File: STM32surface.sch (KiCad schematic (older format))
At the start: 25 parts, among them J3 USB_B, J4 Conn_01x04, J5 Conn_01x20, J6 Conn_02x03_Odd_Even, J7 Conn_01x02, J9 Conn_01x20, U1 AMS1117-3V3, U2 STM32F103C8T6, Y1 8 MHz, Y2 Crystal

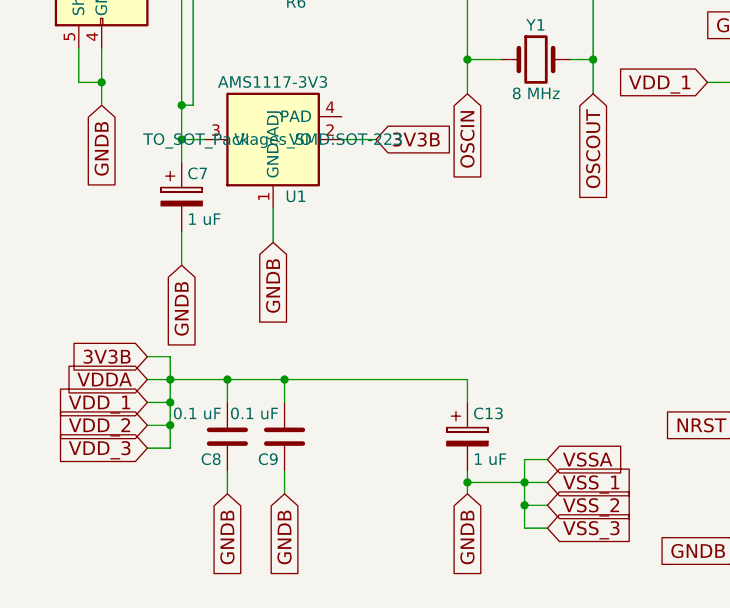
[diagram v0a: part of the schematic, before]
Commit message: Changed all to JLCPCB parts
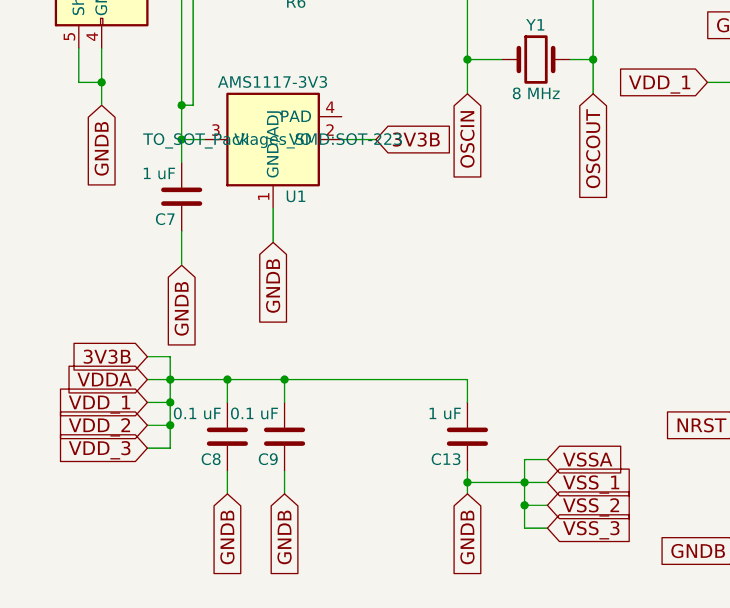
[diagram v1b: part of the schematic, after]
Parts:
- removed C13, C7: 1 uF, Capacitors_SMD:CP_Elec_3x5.3, symbol CP
- added C13, C7: 1 uF, Capacitors_SMD:C_0805_HandSoldering, symbol C
- C12, C14, C15, C16: LCSC (none) -> C1804
- C17: LCSC (none) -> C1710
- C8, C9: LCSC (none) -> C49678
- D4: LCSC (none) -> C2296
- R11: LCSC (none) -> C17710
- R3, R9: LCSC (none) -> C4310
- R4, R6: LCSC (none) -> C17561
- U1: LCSC (none) -> C6186
- U2: LCSC (none) -> C8304
- Y1: footprint Crystals:Crystal_HC49-U_Vertical -> Crystals:Crystal_SMD_5032-2pin_5.0x3.2mm; LCSC (none) -> C115962
- Y2: footprint Crystals:Crystal_Round_d2.0mm_Vertical -> Crystals:Crystal_SMD_3215-2pin_3.2x1.5mm; LCSC (none) -> C32346
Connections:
- net 3V3B: now also C13.2
- net 5VB: now also C7.2
- net GNDB: now also C13.1, C7.1
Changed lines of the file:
@@
 F 2 "Housings_QFP:LQFP-48_7x7mm_Pitch0.5mm" H 6050 2600 60  0001 C CNN
 F 3 "" H 6050 2600 60  0001 C CNN
+F 4 "C8304" H 5850 2600 60  0001 C CNN "LCSC"
 	1    5850 2600
 	1    0    0    -1
@@
 F 0 "Y1" H 4850 5400 50  0000 C CNN
 F 1 "8 MHz" H 4850 5100 50  0000 C CNN
-F 2 "Crystals:Crystal_HC49-U_Vertical" H 4850 5250 50  0001 C CNN
+F 2 "Crystals:Crystal_SMD_5032-2pin_5.0x3.2mm" H 4850 5250 50  0001 C CNN
 F 3 "" H 4850 5250 50  0001 C CNN
+F 4 "C115962" H 4850 5250 60  0001 C CNN "LCSC"
 	1    4850 5250
 	1    0    0    -1
@@
 F 2 "Capacitors_SMD:C_0805_HandSoldering" H 4588 4500 50  0001 C CNN
 F 3 "" H 4550 4650 50  0001 C CNN
+F 4 "C1804" H 4550 4650 60  0001 C CNN "LCSC"
 	1    4550 4650
 	-1   0    0    1
@@
 F 2 "Capacitors_SMD:C_0805_HandSoldering" H 5138 4500 50  0001 C CNN
 F 3 "" H 5100 4650 50  0001 C CNN
+F 4 "C1804" H 5100 4650 60  0001 C CNN "LCSC"
 	1    5100 4650
 	-1   0    0    1
@@
 F 2 "Resistors_SMD:R_0805_HandSoldering" V 3730 4800 50  0001 C CNN
 F 3 "" H 3800 4800 50  0001 C CNN
+F 4 "C17561" V 3800 4800 60  0001 C CNN "LCSC"
 	1    3800 4800
 	0    1    -1   0
@@
 F 2 "Resistors_SMD:R_0805_HandSoldering" V 3730 4900 50  0001 C CNN
 F 3 "" H 3800 4900 50  0001 C CNN
+F 4 "C17561" V 3800 4900 60  0001 C CNN "LCSC"
 	1    3800 4900
 	0    1    -1   0
@@
 F 2 "Resistors_SMD:R_0805_HandSoldering" V 3530 4550 50  0001 C CNN
 F 3 "" H 3600 4550 50  0001 C CNN
+F 4 "C4310" V 3600 4550 60  0001 C CNN "LCSC"
 	1    3600 4550
 	-1   0    0    -1
@@
 Text GLabel 4150 5600 2    60   Input ~ 0
 3V3B
-$Comp
-L CP C7
-U 1 1 5B2088DE
-P 3300 5850
-F 0 "C7" H 3325 5950 50  0000 L CNN
-F 1 "1 uF" H 3325 5750 50  0000 L CNN
-F 2 "Capacitors_SMD:CP_Elec_3x5.3" H 3338 5700 50  0001 C CNN
-F 3 "" H 3300 5850 50  0001 C CNN
-	1    3300 5850
-	1    0    0    -1
-$EndComp
 Text GLabel 3300 6150 3    60   Input ~ 0
 GNDB
@@
 F 2 "Capacitors_SMD:C_0805_HandSoldering" H 3538 6750 50  0001 C CNN
 F 3 "" H 3500 6900 50  0001 C CNN
+F 4 "C49678" H 3500 6900 60  0001 C CNN "LCSC"
 	1    3500 6900
 	-1   0    0    1
@@
 F 2 "Capacitors_SMD:C_0805_HandSoldering" H 3788 6750 50  0001 C CNN
 F 3 "" H 3750 6900 50  0001 C CNN
+F 4 "C49678" H 3750 6900 60  0001 C CNN "LCSC"
 	1    3750 6900
 	-1   0    0    1
@@
 Text GLabel 3750 7150 3    60   Input ~ 0
 GNDB
-$Comp
-L CP C13
-U 1 1 5B20A7CD
-P 4550 6900
-F 0 "C13" H 4575 7000 50  0000 L CNN
-F 1 "1 uF" H 4575 6800 50  0000 L CNN
-F 2 "Capacitors_SMD:CP_Elec_3x5.3" H 4588 6750 50  0001 C CNN
-F 3 "" H 4550 6900 50  0001 C CNN
-	1    4550 6900
-	1    0    0    -1
-$EndComp
 Text GLabel 4550 7150 3    60   Input ~ 0
 GNDB
@@
 F 2 "LEDs:LED_0805_HandSoldering" H 6050 5700 50  0001 C CNN
 F 3 "" H 6050 5700 50  0001 C CNN
+F 4 "C2296" H 6050 5700 60  0001 C CNN "LCSC"
 	1    6050 5700
 	0    -1   -1   0
@@
 F 2 "Resistors_SMD:R_0805_HandSoldering" V 5980 6100 50  0001 C CNN
 F 3 "" H 6050 6100 50  0001 C CNN
+F 4 "C17710" V 6050 6100 60  0001 C CNN "LCSC"
 	1    6050 6100
 	1    0    0    1
@@
 F 0 "Y2" H 5800 950 50  0000 C CNN
 F 1 "Crystal" H 5800 650 50  0000 C CNN
-F 2 "Crystals:Crystal_Round_d2.0mm_Vertical" H 5800 800 50  0001 C CNN
+F 2 "Crystals:Crystal_SMD_3215-2pin_3.2x1.5mm" H 5800 800 50  0001 C CNN
 F 3 "" H 5800 800 50  0001 C CNN
+F 4 "C32346" H 5800 800 60  0001 C CNN "LCSC"
 	1    5800 800
 	0    -1   -1   0
@@
 F 2 "Capacitors_SMD:C_0805_HandSoldering" H 6088 450 50  0001 C CNN
 F 3 "" H 6050 600 50  0001 C CNN
+F 4 "C1804" H 6050 600 60  0001 C CNN "LCSC"
 	1    6050 600
 	0    -1   -1   0
@@
 F 2 "Capacitors_SMD:C_0805_HandSoldering" H 6088 850 50  0001 C CNN
 F 3 "" H 6050 1000 50  0001 C CNN
+F 4 "C1804" H 6050 1000 60  0001 C CNN "LCSC"
 	1    6050 1000
 	0    -1   -1   0
@@
 F 2 "Capacitors_SMD:C_0805_HandSoldering" H 5938 6850 50  0001 C CNN
 F 3 "" H 5900 7000 50  0001 C CNN
+F 4 "C1710" H 5900 7000 60  0001 C CNN "LCSC"
 	1    5900 7000
 	1    0    0    -1
@@
 F 2 "Resistors_SMD:R_0805_HandSoldering" V 6230 6850 50  0001 C CNN
 F 3 "" H 6300 6850 50  0001 C CNN
+F 4 "C4310" V 6300 6850 60  0001 C CNN "LCSC"
 	1    6300 6850
 	0    1    -1   0
@@
 F 5 "Texas Instruments" H 3900 5450 61  0001 C CNN "MFG_NAME"
 F 6 "LM1117" H 4000 5550 61  0001 C CNN "MPN"
+F 7 "C6186" H 3700 5600 60  0001 C CNN "LCSC"
 	1    3700 5600
 	1    0    0    -1
 $EndComp
+$Comp
+L C C13
+U 1 1 5EF169B4
+P 4550 6900
+F 0 "C13" H 4575 7000 50  0000 L CNN
+F 1 "1 uF" H 4575 6800 50  0000 L CNN
+F 2 "Capacitors_SMD:C_0805_HandSoldering" H 4588 6750 50  0001 C CNN
+F 3 "" H 4550 6900 50  0001 C CNN
+F 4 "C28323" H 4550 6900 60  0001 C CNN "LCSC"
+	1    4550 6900
+	-1   0    0    1
+$EndComp
+$Comp
+L C C7
+U 1 1 5EF17365
+P 3300 5850
+F 0 "C7" H 3325 5950 50  0000 L CNN
+F 1 "1 uF" H 3325 5750 50  0000 L CNN
+F 2 "Capacitors_SMD:C_0805_HandSoldering" H 3338 5700 50  0001 C CNN
+F 3 "" H 3300 5850 50  0001 C CNN
+F 4 "C28323" H 3300 5850 60  0001 C CNN "LCSC"
+	1    3300 5850
+	-1   0    0    1
+$EndComp
 $EndSCHEMATC
